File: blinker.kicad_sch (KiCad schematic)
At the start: 31 parts, among them J1 SH1.0 Female, SW1 SW_Push, SW2 SW_DPDT_x2, U1 STM32L433CBTx, U2 STM32F103C8T6, Y1 Crystal

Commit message: switch thingy
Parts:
- added SW3: SW_DPDT_x2, Switches:SWITCH_SPDT_PTH_11.6X4.0MM_LOCK, symbol Switch:SW_DPDT_x2
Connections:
- net +3V3: now also SW3.1 (A)
- net PROG3V3: now also SW3.3 (C)
- net at C5.1, C6.1, C7.1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: now also SW3.2 (B)
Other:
- moved on the sheet: C1, C2, C3, C4, C5, C6, C7, D1, D2, D3, D4, D5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

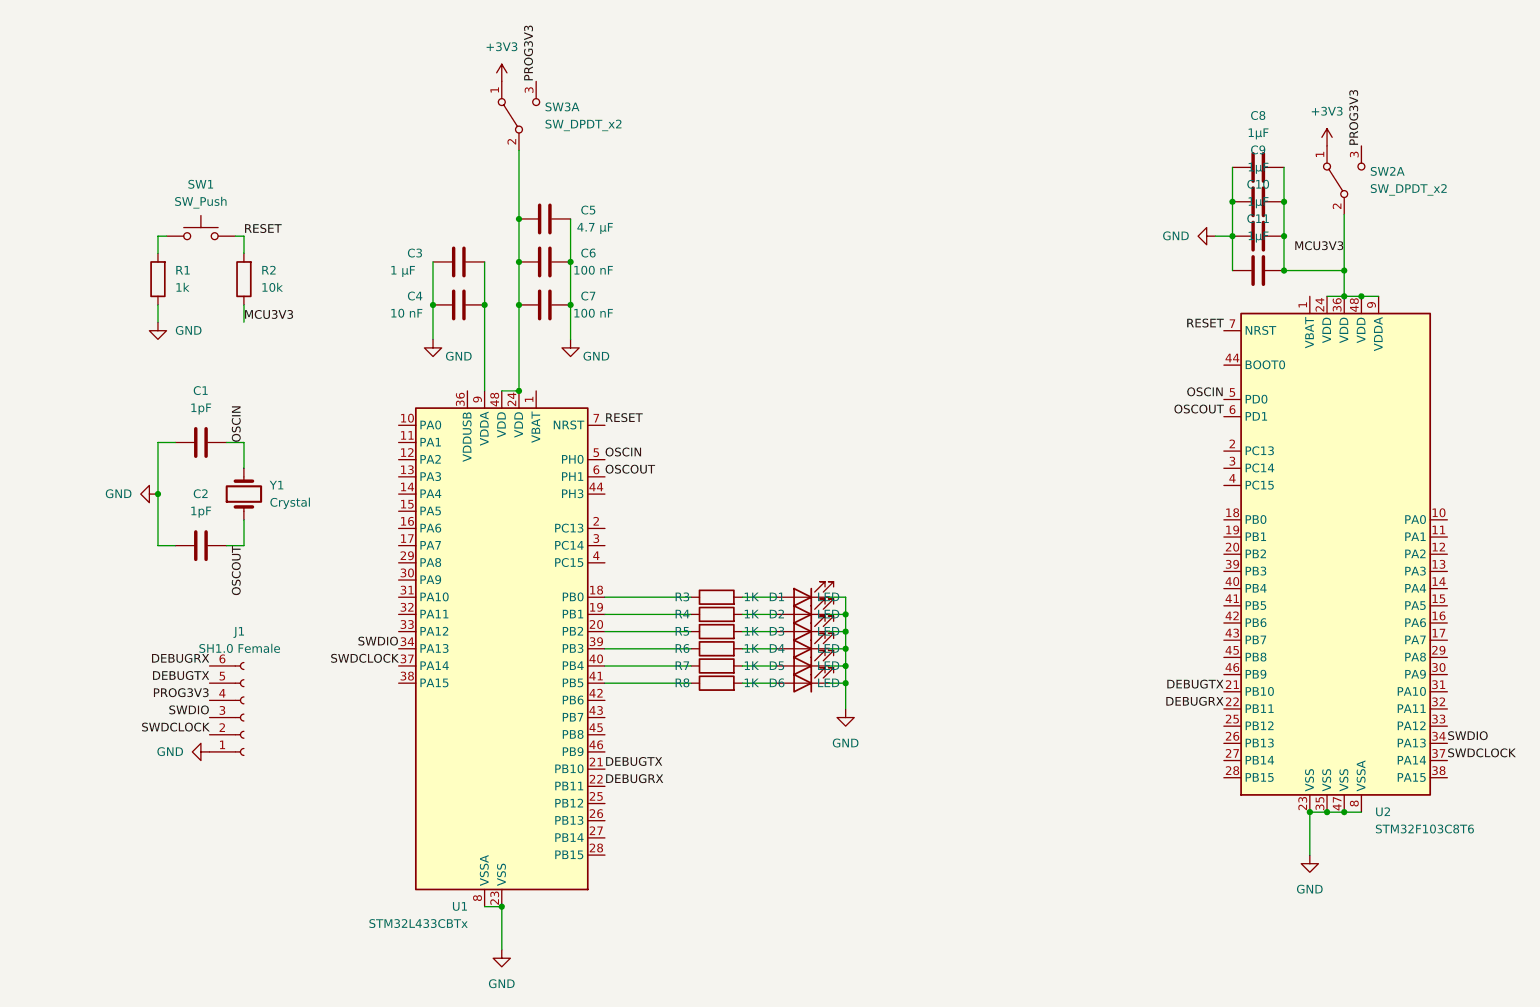
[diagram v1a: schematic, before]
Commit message: battery holder schema
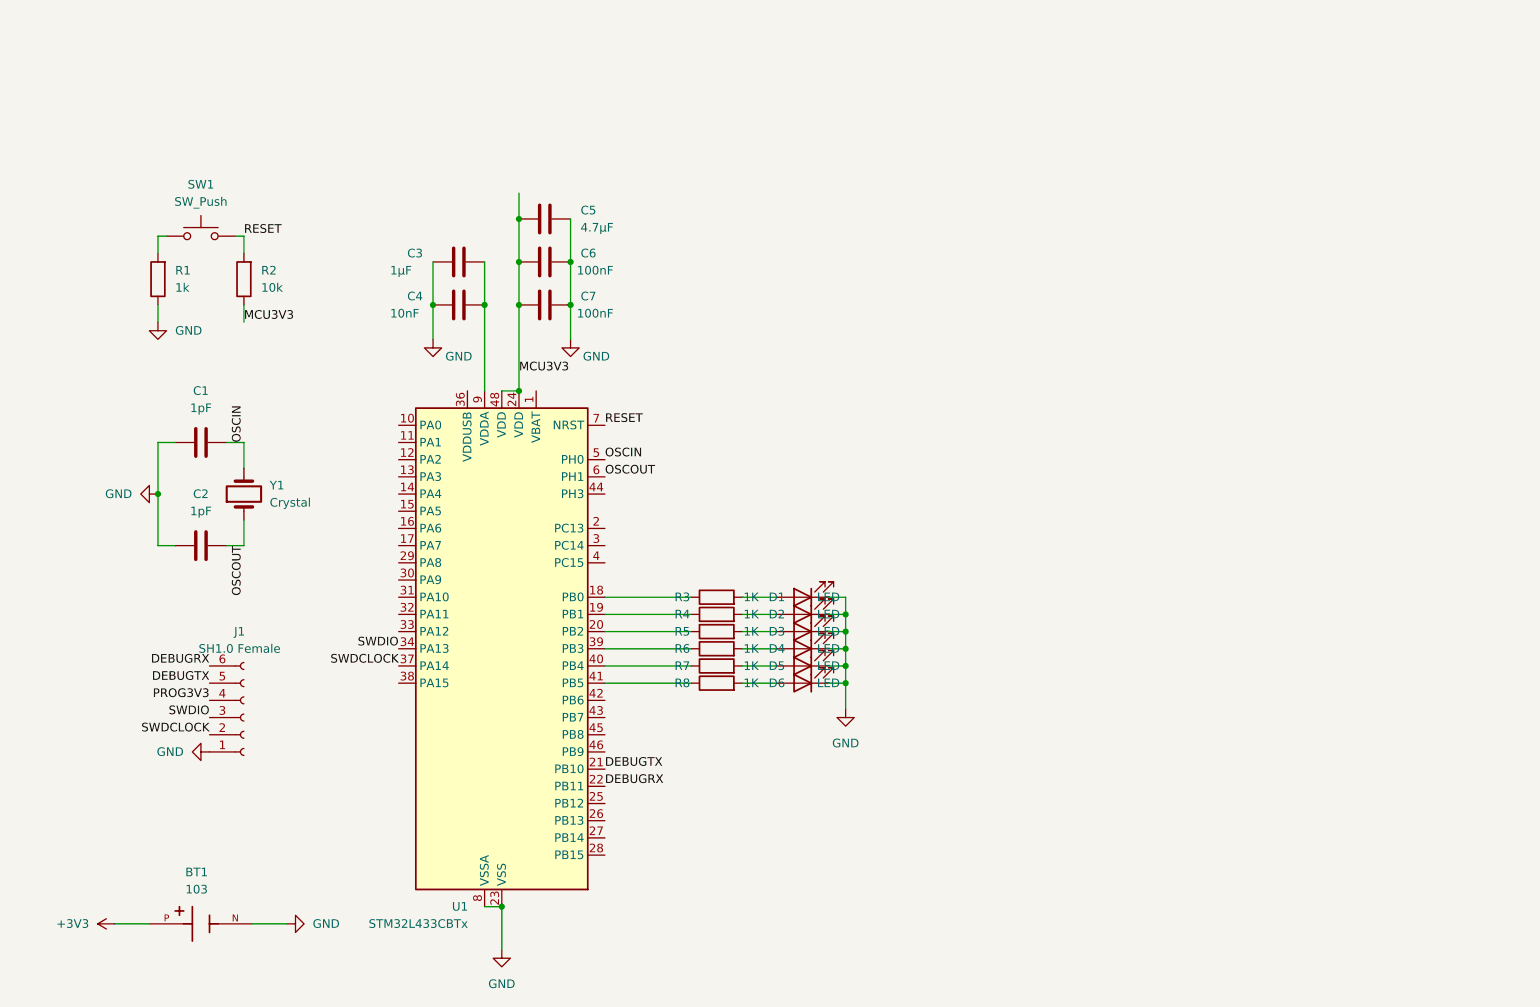
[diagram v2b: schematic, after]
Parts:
- removed C10, C11, C8, C9: 1μF, Capacitor_SMD:C_0603_1608Metric, symbol Device:C
- removed SW2, SW3: SW_DPDT_x2, Switches:SWITCH_SPDT_PTH_11.6X4.0MM_LOCK, symbol Switch:SW_DPDT_x2
- removed U2: STM32F103C8T6, Package_QFP:LQFP-48_7x7mm_P0.5mm, symbol MCU_ST_STM32F1:STM32F103C8Tx
- added BT1: 103, Battery:BatteryHolder_Keystone_103_1x20mm, symbol 103:103
- C3: value 1 µF -> 1µF; footprint (none) -> Capacitor_SMD:C_0603_1608Metric
- C4: value 10 nF -> 10nF; footprint (none) -> Capacitor_SMD:C_0603_1608Metric
- C5: value 4.7 µF -> 4.7µF; footprint (none) -> Capacitor_SMD:C_0603_1608Metric
- C6, C7: value 100 nF -> 100nF; footprint (none) -> Capacitor_SMD:C_0603_1608Metric
- D1, D2, D3, D4, D5, D6: footprint (none) -> LED_SMD:LED_0603_1608Metric
- R3, R4, R5, R6, R7, R8: footprint (none) -> Resistor_SMD:R_0603_1608Metric
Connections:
- net +3V3: now also BT1.P
- net GND: now also BT1.N
- net MCU3V3: now also C5.1, C6.1, C7.1, U1.24 (VDD), U1.48 (VDD)

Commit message: gerber
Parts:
- BT1: footprint Battery:BatteryHolder_Keystone_103_1x20mm -> footprints:BAT_103
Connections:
- net MCU3V3 is gone; now on net +3V3: C5.1, C6.1, C7.1, R2.1, U1.24 (VDD), U1.48 (VDD)
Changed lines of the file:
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@@
     (effects (font (size 1.27 1.27)) (justify right bottom))
+  )
+  (symbol (lib_id "power:+3V3") (at 91.44 44.45 0) (unit 1)
+    (in_bom yes) (on_board yes) (dnp no) (fields_autoplaced)
+    (property "Reference" "#PWR07" (at 91.44 48.26 0)
+      (effects (font (size 1.27 1.27)) hide)
+    )
+    (property "Value" "+3V3" (at 91.44 39.37 0)
+      (effects (font (size 1.27 1.27)))
+    )
+    (property "Footprint" "" (at 91.44 44.45 0)
+      (effects (font (size 1.27 1.27)) hide)
+    )
+    (property "Datasheet" "" (at 91.44 44.45 0)
+      (effects (font (size 1.27 1.27)) hide)
+    )
+    (pin "1")
+    (instances
+      (project "blinker"
+        (path "/98b7b6ee-d8cc-497d-b35e-1c304e1f06ea"
+          (reference "#PWR07") (unit 1)
+        )
+      )
+    )
   )
   (symbol (lib_id "Device:LED") (at 133.35 104.14 180) (unit 1)
@@
       (effects (font (size 1.27 1.27)))
     )
-    (property "Footprint" "Battery:BatteryHolder_Keystone_103_1x20mm" (at 44.45 152.4 0)
+    (property "Footprint" "footprints:BAT_103" (at 44.45 152.4 0)
       (effects (font (size 1.27 1.27)) (justify bottom) hide)
     )
